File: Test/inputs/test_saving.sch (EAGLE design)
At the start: 8 parts

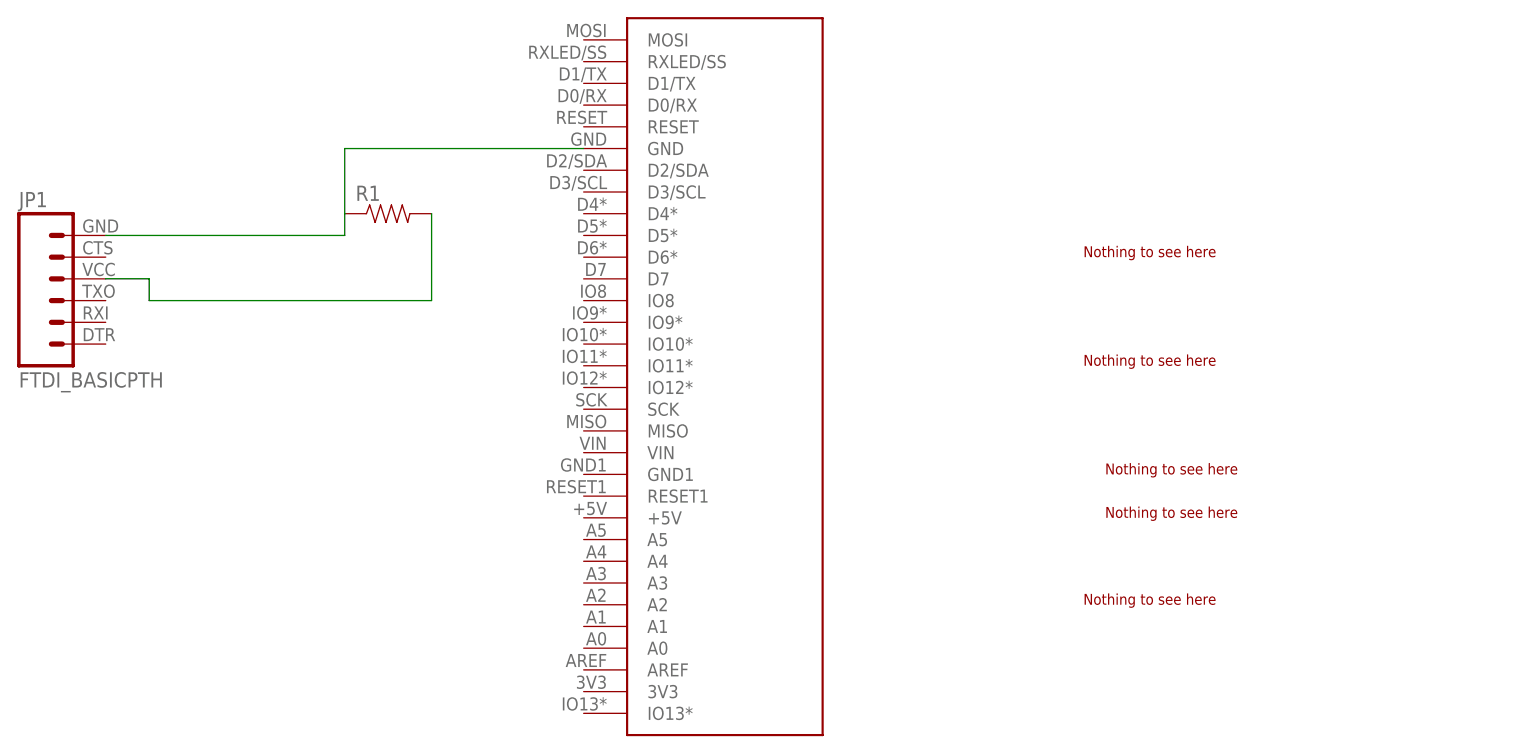
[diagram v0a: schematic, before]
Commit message: Major improvements to bounding boxes. Now supports: arcs (with width), long pads, offset pads, rotated offset/long pads, rotated octagons. With tests.
git-svn-id: svn+ssh://bbfs-01.calit2.net/grw/Gordon/svn/trunk/Gadgets/Tools/CircuitsByCode@20711 2cf53259-273a-af40-bda6-69d31023b8ec
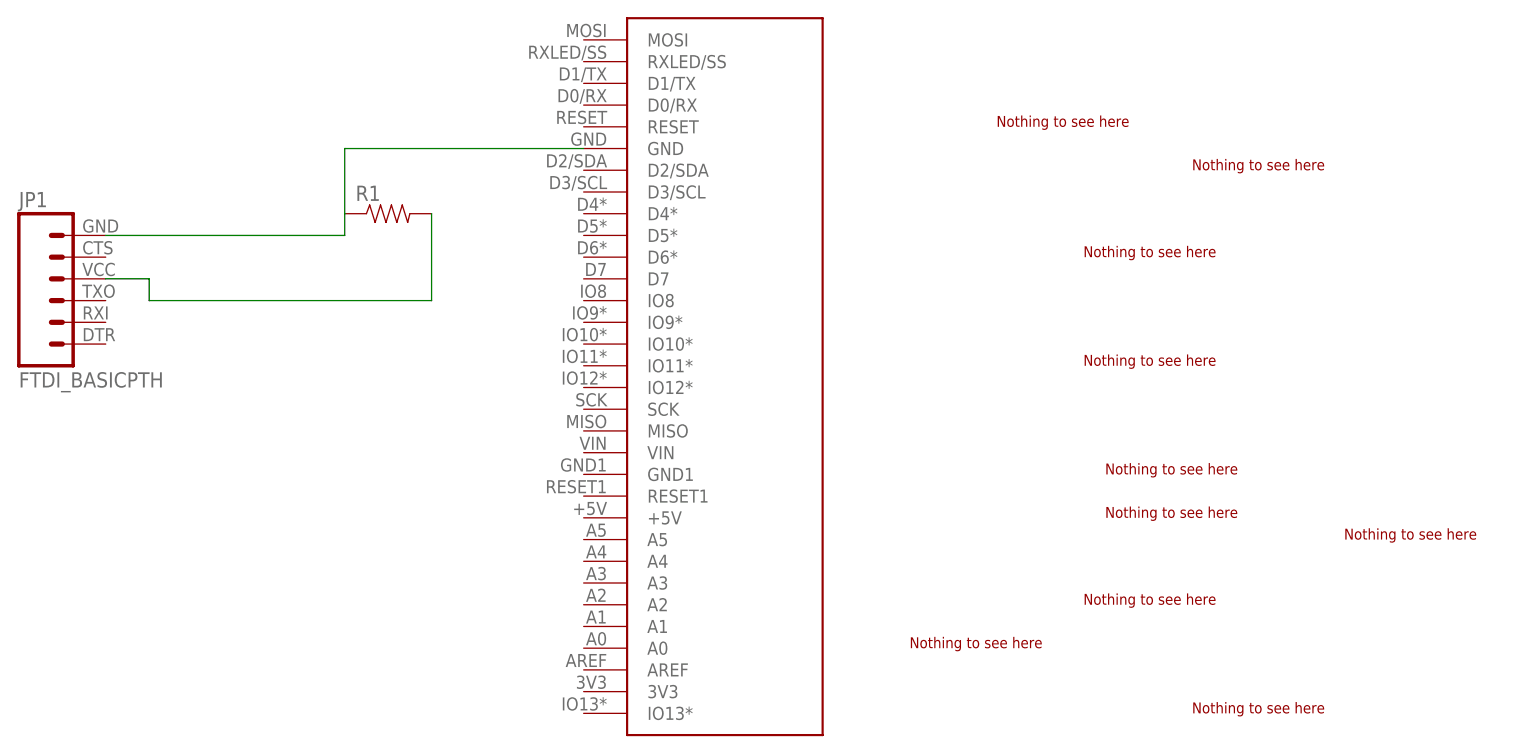
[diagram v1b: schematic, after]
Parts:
- added TEST-ARC3: TEST-ARC3, Swoop-Test-Packages:TEST-ARC3
- added TEST-PAD-OCT: TEST-PAD-OCT, Swoop-Test-Packages:TEST-PAD-OCT
- added TEST-PAD-OCT2: TEST-PAD-OCT2, Swoop-Test-Packages:TEST-PAD-OCT2
- added TEST-PAD-ROT: TEST-PAD-ROT, Swoop-Test-Packages:TEST-PAD-ROT
- added TEST-PAD-SQUARE-ROT: TEST-PAD-SQUARE-ROT, Swoop-Test-Packages:TEST-PAD-SQUARE-ROT
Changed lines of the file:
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@@
 <part name="TEST-PAD-SQUARE" library="Swoop-Test-Packages" deviceset="TEST-PAD3" device=""/>
 <part name="TEST-PAD-ROUND" library="Swoop-Test-Packages" deviceset="TEST-PAD-ROUND" device=""/>
+<part name="TEST-ARC3" library="Swoop-Test-Packages" deviceset="TEST-ARC3" device=""/>
+<part name="TEST-PAD-ROT" library="Swoop-Test-Packages" deviceset="TEST-PAD-ROT" device=""/>
+<part name="TEST-PAD-OCT" library="Swoop-Test-Packages" deviceset="TEST-PAD-OCT" device=""/>
+<part name="TEST-PAD-SQUARE-ROT" library="Swoop-Test-Packages" deviceset="TEST-PAD-SQUARE-ROT" device=""/>
+<part name="TEST-PAD-OCT2" library="Swoop-Test-Packages" deviceset="TEST-PAD-OCT2" device=""/>
 </parts>
 <sheets>
@@
 <instance part="TEST-PAD-SQUARE" gate="G$1" x="157.48" y="30.48"/>
 <instance part="TEST-PAD-ROUND" gate="G$1" x="154.94" y="20.32"/>
+<instance part="TEST-ARC3" gate="G$1" x="144.78" y="76.2"/>
+<instance part="TEST-PAD-ROT" gate="G$1" x="167.64" y="7.62"/>
+<instance part="TEST-PAD-OCT" gate="G$1" x="134.62" y="15.24"/>
+<instance part="TEST-PAD-SQUARE-ROT" gate="G$1" x="167.64" y="71.12"/>
+<instance part="TEST-PAD-OCT2" gate="G$1" x="185.42" y="27.94"/>
 </instances>
 <busses>

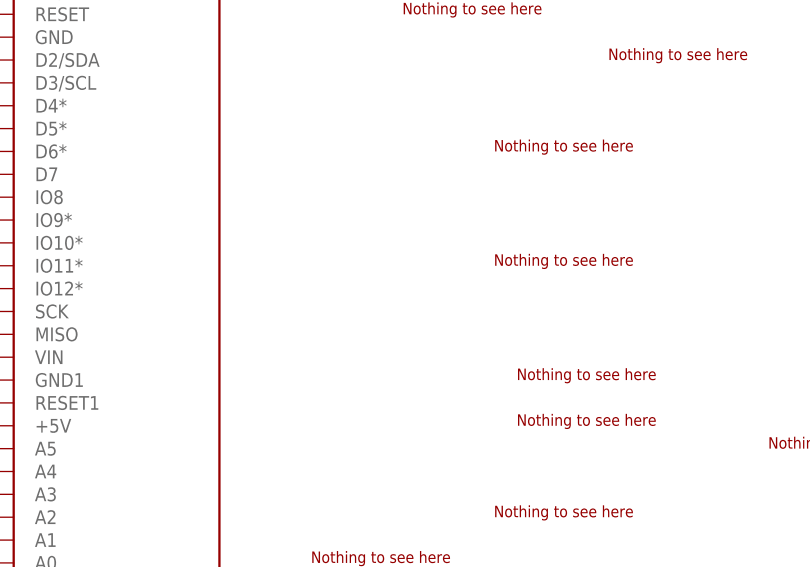
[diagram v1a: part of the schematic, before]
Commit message: Added holes and circles
git-svn-id: svn+ssh://bbfs-01.calit2.net/grw/Gordon/svn/trunk/Gadgets/Tools/CircuitsByCode@20788 2cf53259-273a-af40-bda6-69d31023b8ec
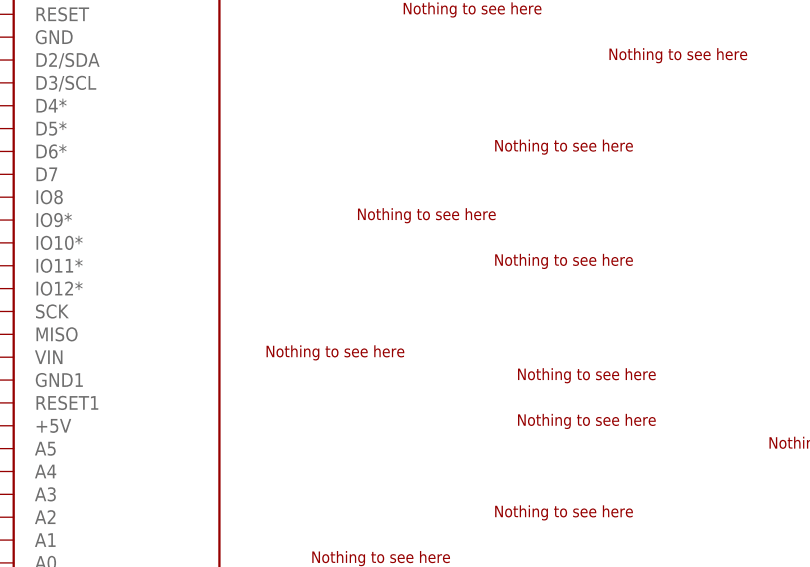
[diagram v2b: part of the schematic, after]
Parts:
- added TEST-CIRCLE: TEST-CIRCLE, Swoop-Test-Packages:TEST-CIRCLE
- added TEST-HOLE: TEST-HOLE, Swoop-Test-Packages:TEST-HOLE
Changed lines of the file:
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@@
 <part name="TEST-PAD-SQUARE-ROT" library="Swoop-Test-Packages" deviceset="TEST-PAD-SQUARE-ROT" device=""/>
 <part name="TEST-PAD-OCT2" library="Swoop-Test-Packages" deviceset="TEST-PAD-OCT2" device=""/>
+<part name="TEST-CIRCLE" library="Swoop-Test-Packages" deviceset="TEST-CIRCLE" device=""/>
+<part name="TEST-HOLE" library="Swoop-Test-Packages" deviceset="TEST-HOLE" device=""/>
 </parts>
 <sheets>
@@
 <instance part="TEST-PAD-SQUARE-ROT" gate="G$1" x="167.64" y="71.12"/>
 <instance part="TEST-PAD-OCT2" gate="G$1" x="185.42" y="27.94"/>
+<instance part="TEST-CIRCLE" gate="G$1" x="129.54" y="38.1"/>
+<instance part="TEST-HOLE" gate="G$1" x="139.7" y="53.34"/>
 </instances>
 <busses>
